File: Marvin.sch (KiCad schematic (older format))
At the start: 18 parts, among them J1 Arduino_Mega_Header, M1 Motor_DC, M2 Stepper_Motor_bipolar, M3 Stepper_Motor_bipolar, M4 Motor_DC, SW1 Rotary_Encoder, U1 L7805, U2 RoetzerRegler, U3 DM420, U4 DM420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

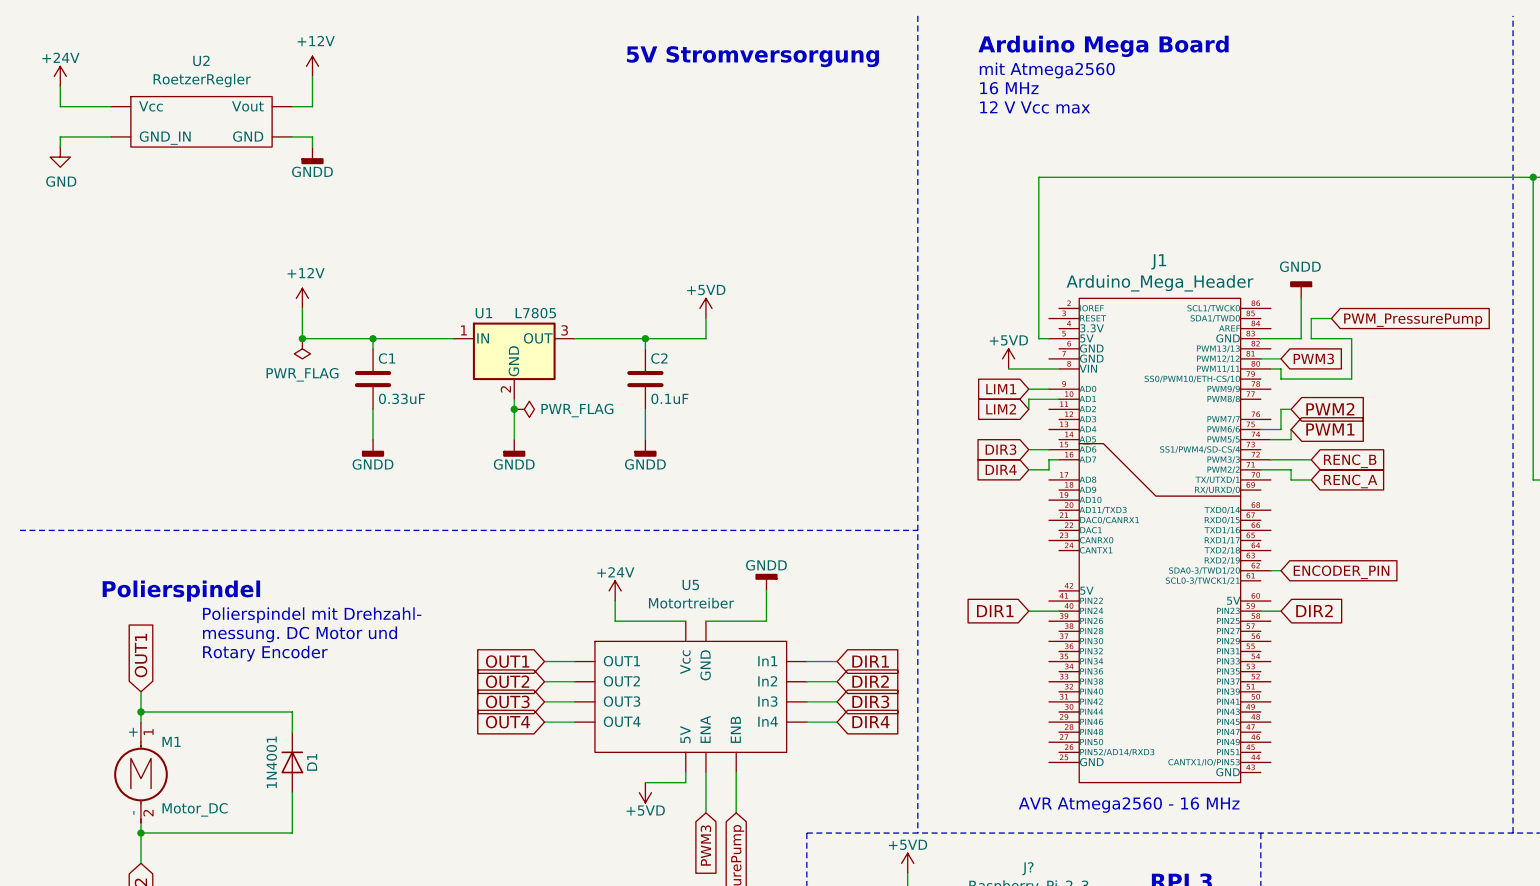
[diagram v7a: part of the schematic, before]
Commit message: Relay Modul
Releis Modul nachgetragen
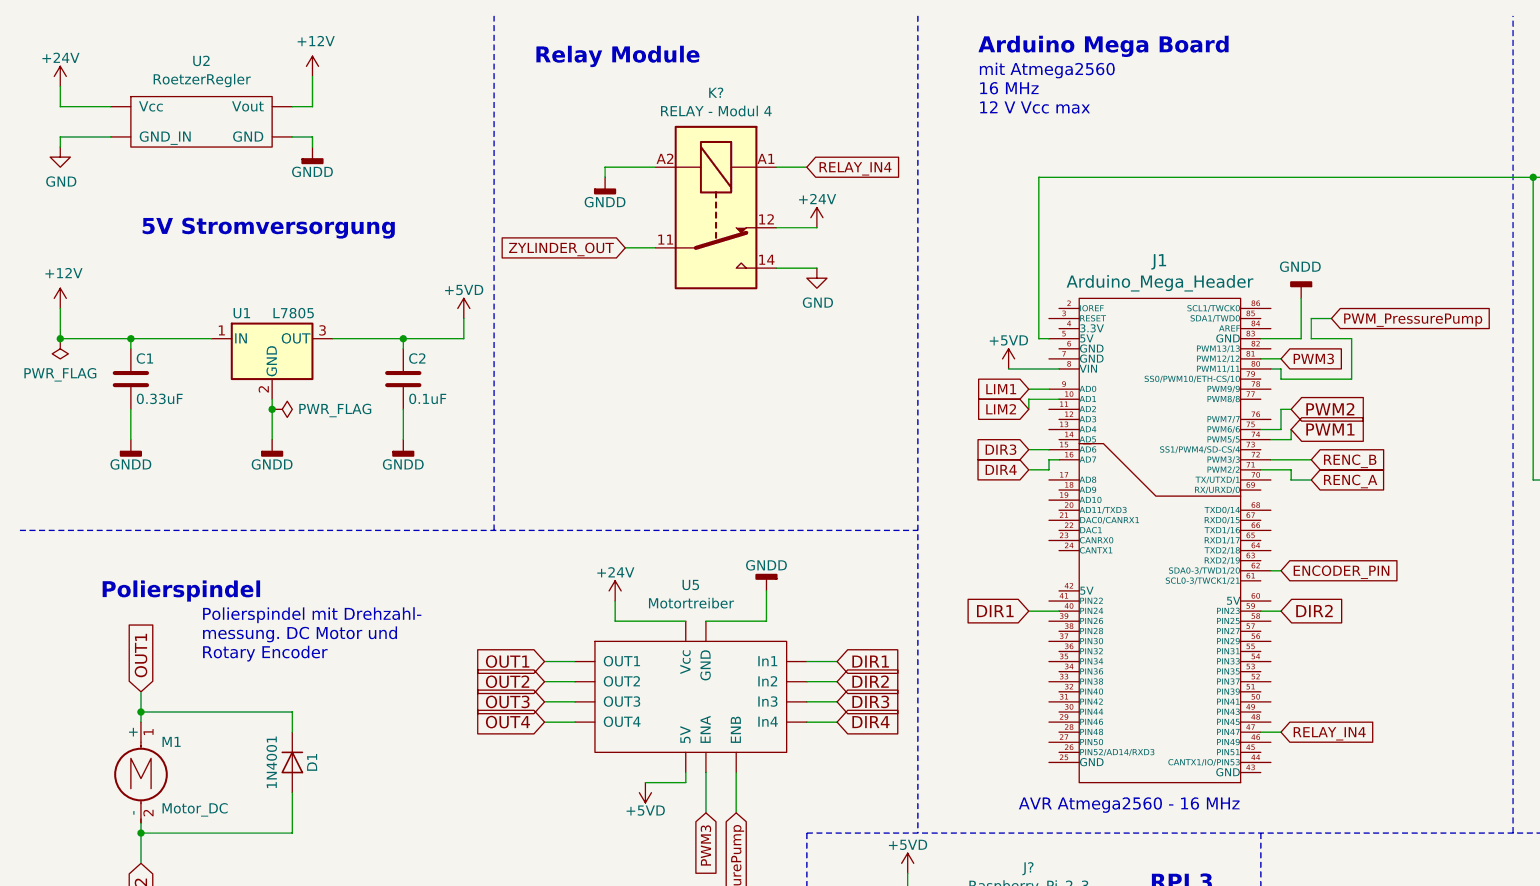
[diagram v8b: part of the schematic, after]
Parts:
- added K?: RELAY - Modul 4, Relay_THT:Relay_SPST_Finder_32.21-x300, symbol Relay:FINDER-32.21-x000
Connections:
- net +24V: now also K?.12
- net GND: now also K?.14
- net GNDD: now also K?.A2
- net RELAY_IN4: now reaches J1.47 (PIN47)
- net RELAY_IN4: now also K?.A1
- new net ZYLINDER_OUT: K?.11
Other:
- note added: "Relay Module"
- moved on the sheet: C1, C2, U1
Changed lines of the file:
@@
 L Marvin-rescue:L7805-regul U1
 U 1 1 5BE05440
-P 2950 2100
-F 0 "U1" H 2800 2225 50  0000 C CNN
-F 1 "L7805" H 2950 2225 50  0000 L CNN
-F 2 "Power_Integrations:TO-220" H 2975 1950 50  0001 L CIN
-F 3 "" H 2950 2050 50  0001 C CNN
-	1    2950 2100
+P 1750 2100
+F 0 "U1" H 1600 2225 50  0000 C CNN
+F 1 "L7805" H 1750 2225 50  0000 L CNN
+F 2 "Power_Integrations:TO-220" H 1775 1950 50  0001 L CIN
+F 3 "" H 1750 2050 50  0001 C CNN
+	1    1750 2100
 	1    0    0    -1
 $EndComp
@@
 L Marvin-rescue:C-Device C1
 U 1 1 5BE054B9
-P 2250 2300
-F 0 "C1" H 2275 2400 50  0000 L CNN
-F 1 "0.33uF" H 2275 2200 50  0000 L CNN
-F 2 "Capacitors_THT:C_Rect_L7.5mm_W6.5mm_P5.00mm" H 2288 2150 50  0001 C CNN
-F 3 "" H 2250 2300 50  0001 C CNN
-	1    2250 2300
+P 1050 2300
+F 0 "C1" H 1075 2400 50  0000 L CNN
+F 1 "0.33uF" H 1075 2200 50  0000 L CNN
+F 2 "Capacitors_THT:C_Rect_L7.5mm_W6.5mm_P5.00mm" H 1088 2150 50  0001 C CNN
+F 3 "" H 1050 2300 50  0001 C CNN
+	1    1050 2300
 	1    0    0    -1
 $EndComp
@@
 L Marvin-rescue:C-Device C2
 U 1 1 5BE05551
-P 3600 2300
-F 0 "C2" H 3625 2400 50  0000 L CNN
-F 1 "0.1uF" H 3625 2200 50  0000 L CNN
-F 2 "Capacitors_THT:C_Rect_L7.5mm_W6.5mm_P5.00mm" H 3638 2150 50  0001 C CNN
-F 3 "" H 3600 2300 50  0001 C CNN
-	1    3600 2300
+P 2400 2300
+F 0 "C2" H 2425 2400 50  0000 L CNN
+F 1 "0.1uF" H 2425 2200 50  0000 L CNN
+F 2 "Capacitors_THT:C_Rect_L7.5mm_W6.5mm_P5.00mm" H 2438 2150 50  0001 C CNN
+F 3 "" H 2400 2300 50  0001 C CNN
+	1    2400 2300
 	1    0    0    -1
 $EndComp
@@
 L Marvin-rescue:GNDD-power #PWR05
 U 1 1 5BE055EE
-P 2950 2600
-F 0 "#PWR05" H 2950 2350 50  0001 C CNN
-F 1 "GNDD" H 2950 2475 50  0000 C CNN
-F 2 "" H 2950 2600 50  0001 C CNN
-F 3 "" H 2950 2600 50  0001 C CNN
-	1    2950 2600
+P 1750 2600
+F 0 "#PWR05" H 1750 2350 50  0001 C CNN
+F 1 "GNDD" H 1750 2475 50  0000 C CNN
+F 2 "" H 1750 2600 50  0001 C CNN
+F 3 "" H 1750 2600 50  0001 C CNN
+	1    1750 2600
 	1    0    0    -1
 $EndComp
@@
 L Marvin-rescue:GNDD-power #PWR03
 U 1 1 5BE0560F
-P 2250 2600
-F 0 "#PWR03" H 2250 2350 50  0001 C CNN
-F 1 "GNDD" H 2250 2475 50  0000 C CNN
-F 2 "" H 2250 2600 50  0001 C CNN
-F 3 "" H 2250 2600 50  0001 C CNN
-	1    2250 2600
+P 1050 2600
+F 0 "#PWR03" H 1050 2350 50  0001 C CNN
+F 1 "GNDD" H 1050 2475 50  0000 C CNN
+F 2 "" H 1050 2600 50  0001 C CNN
+F 3 "" H 1050 2600 50  0001 C CNN
+	1    1050 2600
 	1    0    0    -1
 $EndComp
@@
 L Marvin-rescue:GNDD-power #PWR08
 U 1 1 5BE05629
-P 3600 2600
-F 0 "#PWR08" H 3600 2350 50  0001 C CNN
-F 1 "GNDD" H 3600 2475 50  0000 C CNN
-F 2 "" H 3600 2600 50  0001 C CNN
-F 3 "" H 3600 2600 50  0001 C CNN
-	1    3600 2600
+P 2400 2600
+F 0 "#PWR08" H 2400 2350 50  0001 C CNN
+F 1 "GNDD" H 2400 2475 50  0000 C CNN
+F 2 "" H 2400 2600 50  0001 C CNN
+F 3 "" H 2400 2600 50  0001 C CNN
+	1    2400 2600
 	1    0    0    -1
 $EndComp
@@
 L Marvin-rescue:+5VD-power #PWR09
 U 1 1 5BE05754
-P 3900 2000
-F 0 "#PWR09" H 3900 1850 50  0001 C CNN
-F 1 "+5VD" H 3900 2140 50  0000 C CNN
-F 2 "" H 3900 2000 50  0001 C CNN
-F 3 "" H 3900 2000 50  0001 C CNN
-	1    3900 2000
+P 2700 2000
+F 0 "#PWR09" H 2700 1850 50  0001 C CNN
+F 1 "+5VD" H 2700 2140 50  0000 C CNN
+F 2 "" H 2700 2000 50  0001 C CNN
+F 3 "" H 2700 2000 50  0001 C CNN
+	1    2700 2000
 	1    0    0    -1
 $EndComp
@@
 Polierspindel\n
 Wire Wire Line
-	1900 2100 2250 2100
-Wire Wire Line
-	2250 2150 2250 2100
-Wire Wire Line
-	3600 2150 3600 2100
-Wire Wire Line
-	3250 2100 3600 2100
-Wire Wire Line
-	1900 1950 1900 2100
-Connection ~ 2250 2100
-Wire Wire Line
-	2250 2450 2250 2600
-Wire Wire Line
-	2950 2400 2950 2450
-Wire Wire Line
-	3600 2450 3600 2600
-Wire Wire Line
-	3900 2100 3900 2000
-Connection ~ 3600 2100
+	700  2100 1050 2100
+Wire Wire Line
+	1050 2150 1050 2100
+Wire Wire Line
+	2400 2150 2400 2100
+Wire Wire Line
+	2050 2100 2400 2100
+Wire Wire Line
+	700  1950 700  2100
+Connection ~ 1050 2100
+Wire Wire Line
+	1050 2450 1050 2600
+Wire Wire Line
+	1750 2400 1750 2450
+Wire Wire Line
+	2400 2450 2400 2600
+Wire Wire Line
+	2700 2100 2700 2000
+Connection ~ 2400 2100
 Wire Wire Line
 	8800 2600 8700 2600
@@
 	1850 4550 1850 4350
 Connection ~ 1100 4550
-Text Notes 3500 750  0    79   ~ 16
+Text Notes 1100 1600 0    79   ~ 16
 5V Stromversorgung
 Text Notes 9250 750  0    79   ~ 16
@@
 Treiberstufe DM420\nmit Mikroschrittfähigkeit\n\nDC Input max 36V
 Wire Wire Line
-	2250 2100 2650 2100
-Wire Wire Line
-	3600 2100 3900 2100
+	1050 2100 1450 2100
+Wire Wire Line
+	2400 2100 2700 2100
 Wire Wire Line
 	8000 1300 8700 1300
@@
 L Marvin-rescue:PWR_FLAG-power #FLG0101
 U 1 1 5BE3EC9B
-P 1900 2100
-F 0 "#FLG0101" H 1900 2175 50  0001 C CNN
-F 1 "PWR_FLAG" H 1900 2273 50  0000 C CNN
-F 2 "" H 1900 2100 50  0001 C CNN
-F 3 "~" H 1900 2100 50  0001 C CNN
-	1    1900 2100
+P 700 2100
+F 0 "#FLG0101" H 700 2175 50  0001 C CNN
+F 1 "PWR_FLAG" H 700 2273 50  0000 C CNN
+F 2 "" H 700 2100 50  0001 C CNN
+F 3 "~" H 700 2100 50  0001 C CNN
+	1    700  2100
 	-1   0    0    1
 $EndComp
-Connection ~ 1900 2100
+Connection ~ 700  2100
 Wire Wire Line
 	8800 1200 8700 1200
@@
 L Marvin-rescue:PWR_FLAG-power #FLG0102
 U 1 1 5BE4D3A1
-P 2950 2450
-F 0 "#FLG0102" H 2950 2525 50  0001 C CNN
-F 1 "PWR_FLAG" V 2950 2578 50  0000 L CNN
-F 2 "" H 2950 2450 50  0001 C CNN
-F 3 "~" H 2950 2450 50  0001 C CNN
-	1    2950 2450
+P 1750 2450
+F 0 "#FLG0102" H 1750 2525 50  0001 C CNN
+F 1 "PWR_FLAG" V 1750 2578 50  0000 L CNN
+F 2 "" H 1750 2450 50  0001 C CNN
+F 3 "~" H 1750 2450 50  0001 C CNN
+	1    1750 2450
 	0    1    1    0
 $EndComp
-Connection ~ 2950 2450
-Wire Wire Line
-	2950 2450 2950 2600
+Connection ~ 1750 2450
+Wire Wire Line
+	1750 2450 1750 2600
 Wire Wire Line
 	5400 2250 5650 2250
@@
 L power:+12V #PWR04
 U 1 1 5C7CD482
-P 1900 1950
-F 0 "#PWR04" H 1900 1800 50  0001 C CNN
-F 1 "+12V" H 1915 2123 50  0000 C CNN
-F 2 "" H 1900 1950 50  0001 C CNN
-F 3 "" H 1900 1950 50  0001 C CNN
-	1    1900 1950
+P 700 1950
+F 0 "#PWR04" H 700 1800 50  0001 C CNN
+F 1 "+12V" H 715 2123 50  0000 C CNN
+F 2 "" H 700 1950 50  0001 C CNN
+F 3 "" H 700 1950 50  0001 C CNN
+	1    700  1950
 	1    0    0    -1
 $EndComp
@@
 Wire Wire Line
 	6750 2300 7100 2300
+$Comp
+L Relay:FINDER-32.21-x000 K?
+U 1 1 5C813E0F
+P 3950 1450
+F 0 "K?" V 3383 1450 50  0000 C CNN
+F 1 "RELAY - Modul 4" V 3474 1450 50  0000 C CNN
+F 2 "Relay_THT:Relay_SPST_Finder_32.21-x300" H 5220 1420 50  0001 C CNN
+F 3 "https://gfinder.findernet.com/assets/Series/355/S32EN.pdf" H 3950 1450 50  0001 C CNN
+	1    3950 1450
+	0    1    1    0
+$EndComp
+Text GLabel 6750 4050 2    50   Input ~ 0
+RELAY_IN4
+Wire Wire Line
+	6650 4050 6750 4050
+Text GLabel 4400 1250 2    50   Input ~ 0
+RELAY_IN4
+Wire Wire Line
+	4250 1250 4400 1250
+Wire Wire Line
+	3650 1250 3400 1250
+Wire Wire Line
+	3400 1250 3400 1300
+$Comp
+L Marvin-rescue:GNDD-power #PWR?
+U 1 1 5C824BEE
+P 3400 1300
+F 0 "#PWR?" H 3400 1050 50  0001 C CNN
+F 1 "GNDD" H 3400 1175 50  0000 C CNN
+F 2 "" H 3400 1300 50  0001 C CNN
+F 3 "" H 3400 1300 50  0001 C CNN
+	1    3400 1300
+	1    0    0    -1
+$EndComp
+$Comp
+L Marvin-rescue:+24V-power #PWR?
+U 1 1 5C824C1F
+P 4450 1550
+F 0 "#PWR?" H 4450 1400 50  0001 C CNN
+F 1 "+24V" H 4450 1690 50  0000 C CNN
+F 2 "" H 4450 1550 50  0001 C CNN
+F 3 "" H 4450 1550 50  0001 C CNN
+	1    4450 1550
+	1    0    0    -1
+$EndComp
+Wire Wire Line
+	4450 1550 4250 1550
+$Comp
+L power:GND #PWR?
+U 1 1 5C82A8E7
+P 4450 1750
+F 0 "#PWR?" H 4450 1500 50  0001 C CNN
+F 1 "GND" H 4455 1577 50  0000 C CNN
+F 2 "" H 4450 1750 50  0001 C CNN
+F 3 "" H 4450 1750 50  0001 C CNN
+	1    4450 1750
+	1    0    0    -1
+$EndComp
+Wire Wire Line
+	4250 1750 4450 1750
+Text GLabel 3500 1650 0    50   Input ~ 0
+ZYLINDER_OUT
+Wire Wire Line
+	3650 1650 3500 1650
+Wire Notes Line
+	2850 3050 2850 500
+Text Notes 3050 750  0    79   ~ 16
+Relay Module
 $EndSCHEMATC
